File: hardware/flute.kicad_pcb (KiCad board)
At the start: 2 copper layers, 230 x 20 mm, 32 parts, among them J1 Conn_01x04, SW1 C, SW2 D, SW3 E, SW4 F, SW5 G, SW6 A, SW7 H, SW8 OCTAVE?, U1 W25Q128JVS, Y1 Crystal_GND24

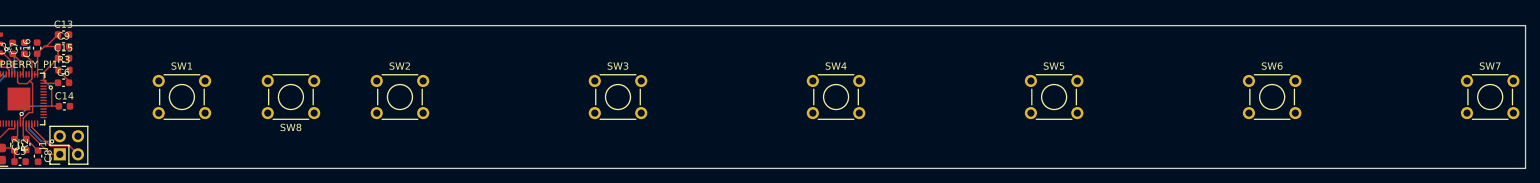
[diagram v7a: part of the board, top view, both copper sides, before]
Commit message: added jack and battery
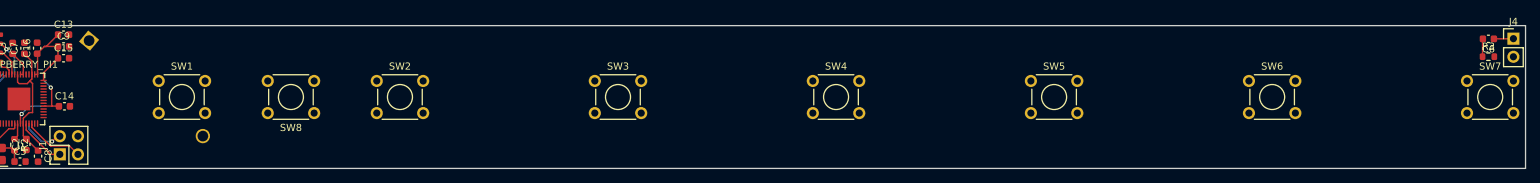
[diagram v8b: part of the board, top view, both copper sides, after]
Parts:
- added BT1: Battery_Cell, Battery:BatteryHolder_MYOUNG_BS-07-A1BJ001_CR2032, B.Cu at (93.0, 122.5)
- added J4: Conn_01x02, Connector_PinHeader_2.54mm:PinHeader_1x02_P2.54mm_Vertical, F.Cu at (292.5, 122.2)
- moved C6 199.7 mm to (289.0, 122.2), turned to 180 degrees
- moved R3 199.5 mm to (289.0, 124.8)
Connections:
- C6 pad 1: Net-(RASPBERRY_PI1-GPIO29_ADC3) -> Net-(J4-Pin_1)
- C6 pad 2: GPIO29 -> /PWM_OUT
- R3 pad 1: GPIO29 -> /PWM_OUT
- RASPBERRY_PI1 pad 41: Net-(RASPBERRY_PI1-GPIO29_ADC3) -> GPIO29
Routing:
- net Net-(J4-Pin_1): track 0.00 -> 2.74 mm
- net /PWM_OUT: track 0.00 -> 2.52 mm
- net GPIO29: track 2.42 -> 0.00 mm
- net Net-(RASPBERRY_PI1-GPIO29_ADC3): track 2.06 -> 0.00 mm
